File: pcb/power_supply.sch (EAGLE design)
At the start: 40 parts, among them P1 2k, Q1 DIODES_FMMT493ATADIODES_FMMT4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, Q2 DIODES_FMMT493ATADIODES_FMMT4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, Q3 DIODES_FMMT493ATADIODES_FMMT4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, Q4 DIODES_FMMT493ATADIODES_FMMT4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, Q5 DIODES_FMMT493ATADIODES_FMMT4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, Q6 DIODES_FMMT493ATADIODES_FMMT4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, Q7 DIODES_FMMT493ATADIODES_FMMT4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, Q8 DIODES_FMMT493ATADIODES_FMMT4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, U1 LM1085IT-ADJ, U2 LM1085IT-ADJ

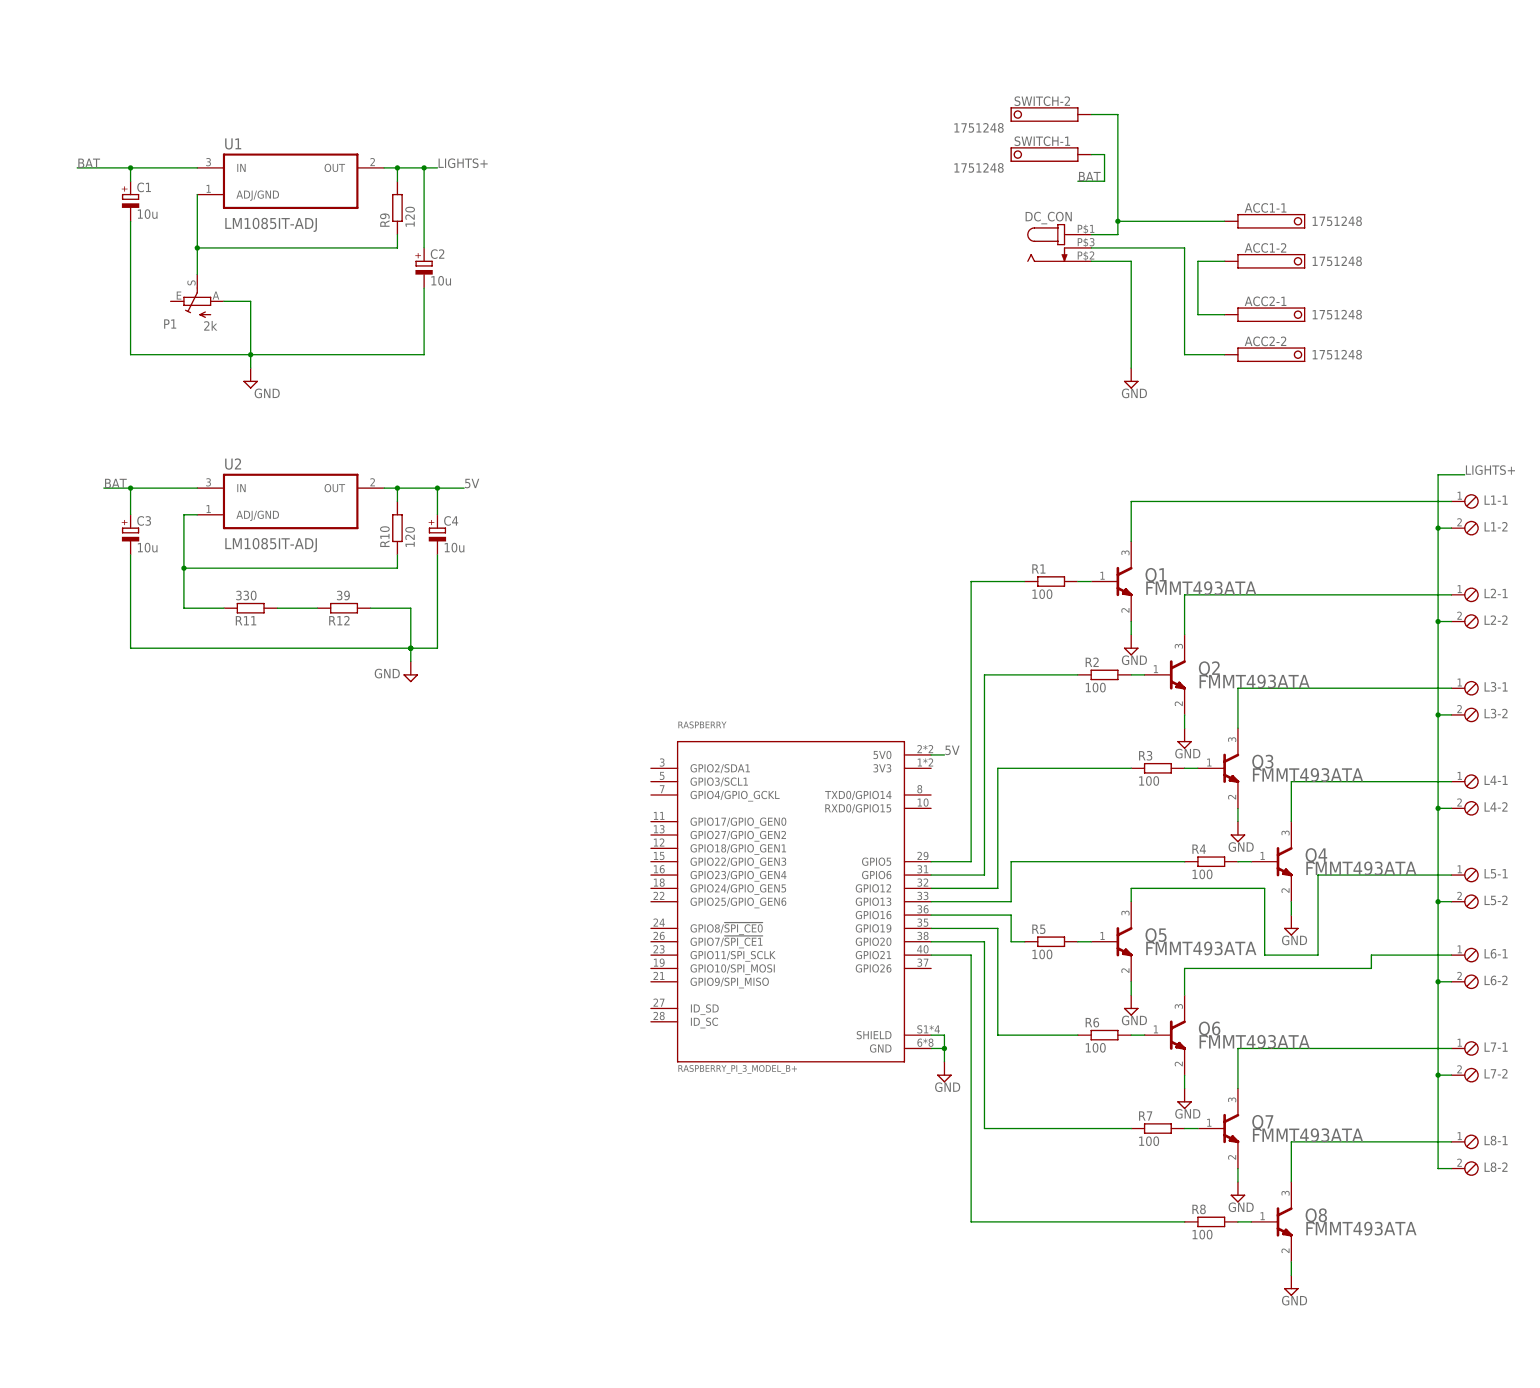
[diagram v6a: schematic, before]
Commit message: pcb - new raspberry supply
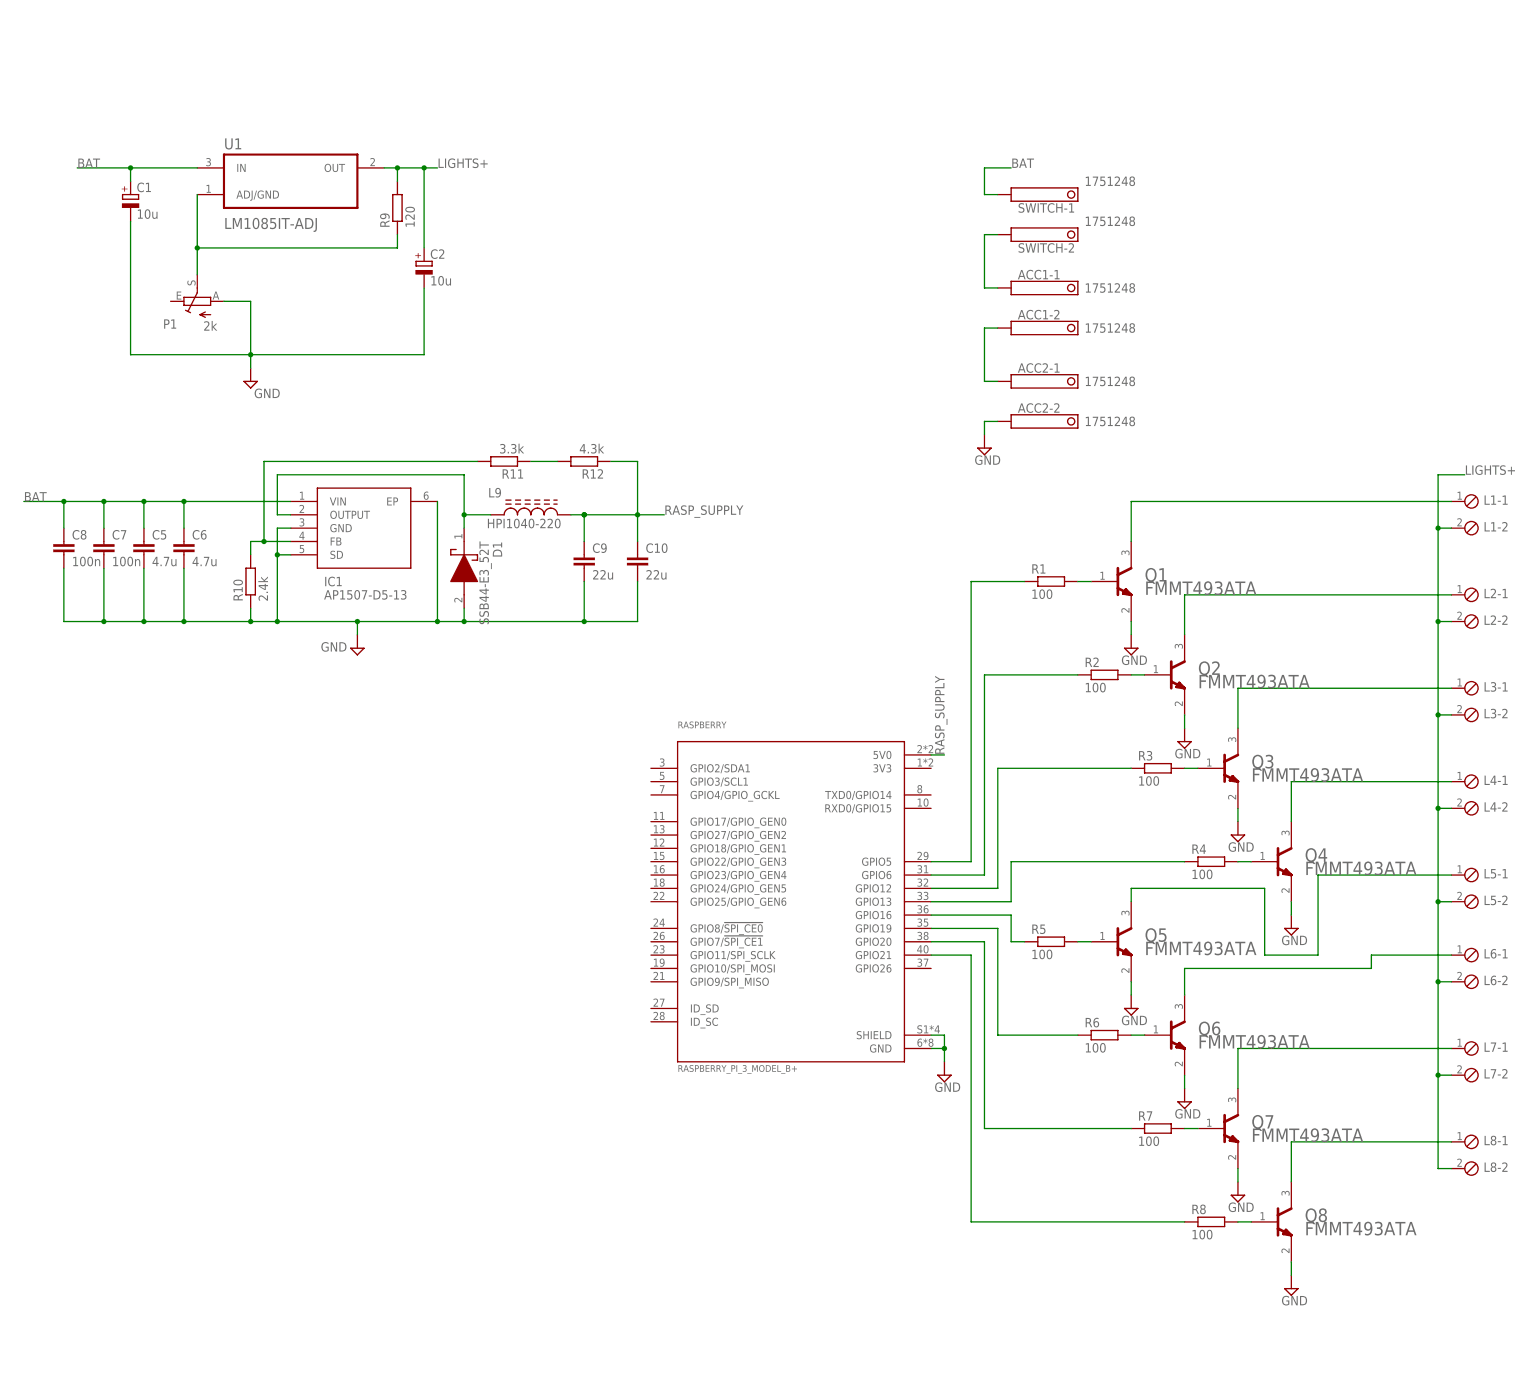
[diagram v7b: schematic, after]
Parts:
- removed C3, C4: 10u, rcl:CPOL-EUB/3528-21R
- removed DC_CON: FC681478WURTH_694106301002, FC681478:FC681478WURTH_694106301002
- removed U2: LM1085IT-ADJ, LM1085IT-ADJ:LM1085IT-ADJ
- added C10, C9: 22u, rcl:C-EUC1206
- added C5, C6: 4.7u, rcl:C-EUC1206
- added C7, C8: 100n, rcl:C-EUC0603
- added D1: SSB44-E3_52T, SSB44-E3_52T:SSB44-E3_52T
- added IC1: AP1507-D5-13, AP1507-D5-13:AP1507-D5-13
- added L9: HPI1040-220, SRR1050A-151Y:SRR1050A-151Y
- R10: value 120 -> 2.4k
- R11: value 330 -> 3.3k
- R12: value 39 -> 4.3k
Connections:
- removed net 5V: C4.+, R10.2, RASPBERRY.5V0, U2.OUT
- removed net N$3: ACC2-2.K, DC_CON.2
- removed net N$31: ACC1-1.K, DC_CON.3, SWITCH-2.K
- new net N$32: D1.K, IC1.OUTPUT, L9.1
- new net RASP_SUPPLY: C10.1, C9.1, IC1.FB, L9.2, R10.2, R11.2, R12.1, RASPBERRY.5V0
- net BAT: now also C5.1, C6.1, C7.1, C8.1, IC1.VIN; no longer C3.+, U2.IN
- net GND: now also ACC2-2.K, C10.2, C5.2, C6.2, C7.2, C8.2, C9.2, D1.A, IC1.EP, IC1.GND, IC1.SD, R10.1; no longer C3.-, C4.-, DC_CON.1, R12.1
- net N$2: now also ACC1-1.K, SWITCH-2.K; no longer R10.1, R11.2, U2.ADJ/GND
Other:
- moved on the sheet: ACC1-1, ACC1-2, ACC2-1, ACC2-2, R10, R11, R12, SWITCH-1, SWITCH-2

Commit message: pcb - schemat updated
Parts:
- added R100: 2.4k, rcl:R-EU_R0805
- added R110: 3.3k, rcl:R-EU_R0805
- added R120, R13, R15: 4.3k, rcl:R-EU_R0805
- added R14, R16: 22k, rcl:R-EU_R0805
- added R90: 120, rcl:R-EU_R0805
- L2, L3, L4, L5, L6, L7, L8: value (none) -> 1
- R1, R3, R5, R7: value 100 -> 4.3k
- R10: value 2.4k -> 22k
- R11: value 3.3k -> 4.3k
- R12: value 4.3k -> 22k
- R2, R4, R6, R8: value 100 -> 22k
- R9: value 120 -> 4.3k
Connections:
- removed net N$11: Q5.B, R5.2
- removed net N$15: Q7.B, R7.2
- removed net N$7: Q3.B, R3.2
- new net N$33: Q6.B, R11.2
- new net N$37: Q7.B, R13.2
- new net N$41: Q8.B, R15.2
- net GND: now also R100.1, R12.1, R14.1, R16.1, R2.1, R4.1, R6.1, R8.1
- net LIGHTS+: now also R90.2; no longer R9.2
- net N$13: now also Q4.B, R7.2; no longer Q6.B, R6.2
- net N$17: now also Q5.B, R9.2; no longer Q8.B, R8.2
- net N$19: now also R2.2
- net N$20: now also R3.1, R4.2; no longer R2.1
- net N$21: now also R5.1, R6.2; no longer R3.1
- net N$23: now also R7.1, R8.2; no longer R4.1
- net N$24: now also R10.2, R9.1; no longer R5.1
- net N$25: now also R11.1, R12.2; no longer R6.1
- net N$26: now also R13.1, R14.2; no longer R7.1
- net N$27: now also R15.1, R16.2; no longer R8.1
- net N$28: now also R110.1, R120.2; no longer R11.1, R12.2
- net N$29: now also R90.1; no longer R9.1
- net N$5: now also R3.2; no longer R2.2
- net N$9: now also Q3.B, R5.2; no longer Q4.B, R4.2
- net RASP_SUPPLY: now also R100.2, R110.2, R120.1; no longer R10.2, R11.2, R12.1
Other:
- moved on the sheet: ACC1-1, ACC1-2, ACC2-1, ACC2-2, C1, C10, C2, C5, C6, C7, C8, C9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
